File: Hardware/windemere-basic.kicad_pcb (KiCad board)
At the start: 2 copper layers, 152.4 x 158.8 mm, 56 parts, among them J3 Connector, J6 Barrel_Jack, SW1 Reset Button, U1 MCP102-475, U2 HD44780U, U3 WD65C02, U4 28C256, U5 62256, U6 WD65C22, U7 74LS00, U8 MM74C923, U9 L7805, X1 1MHz

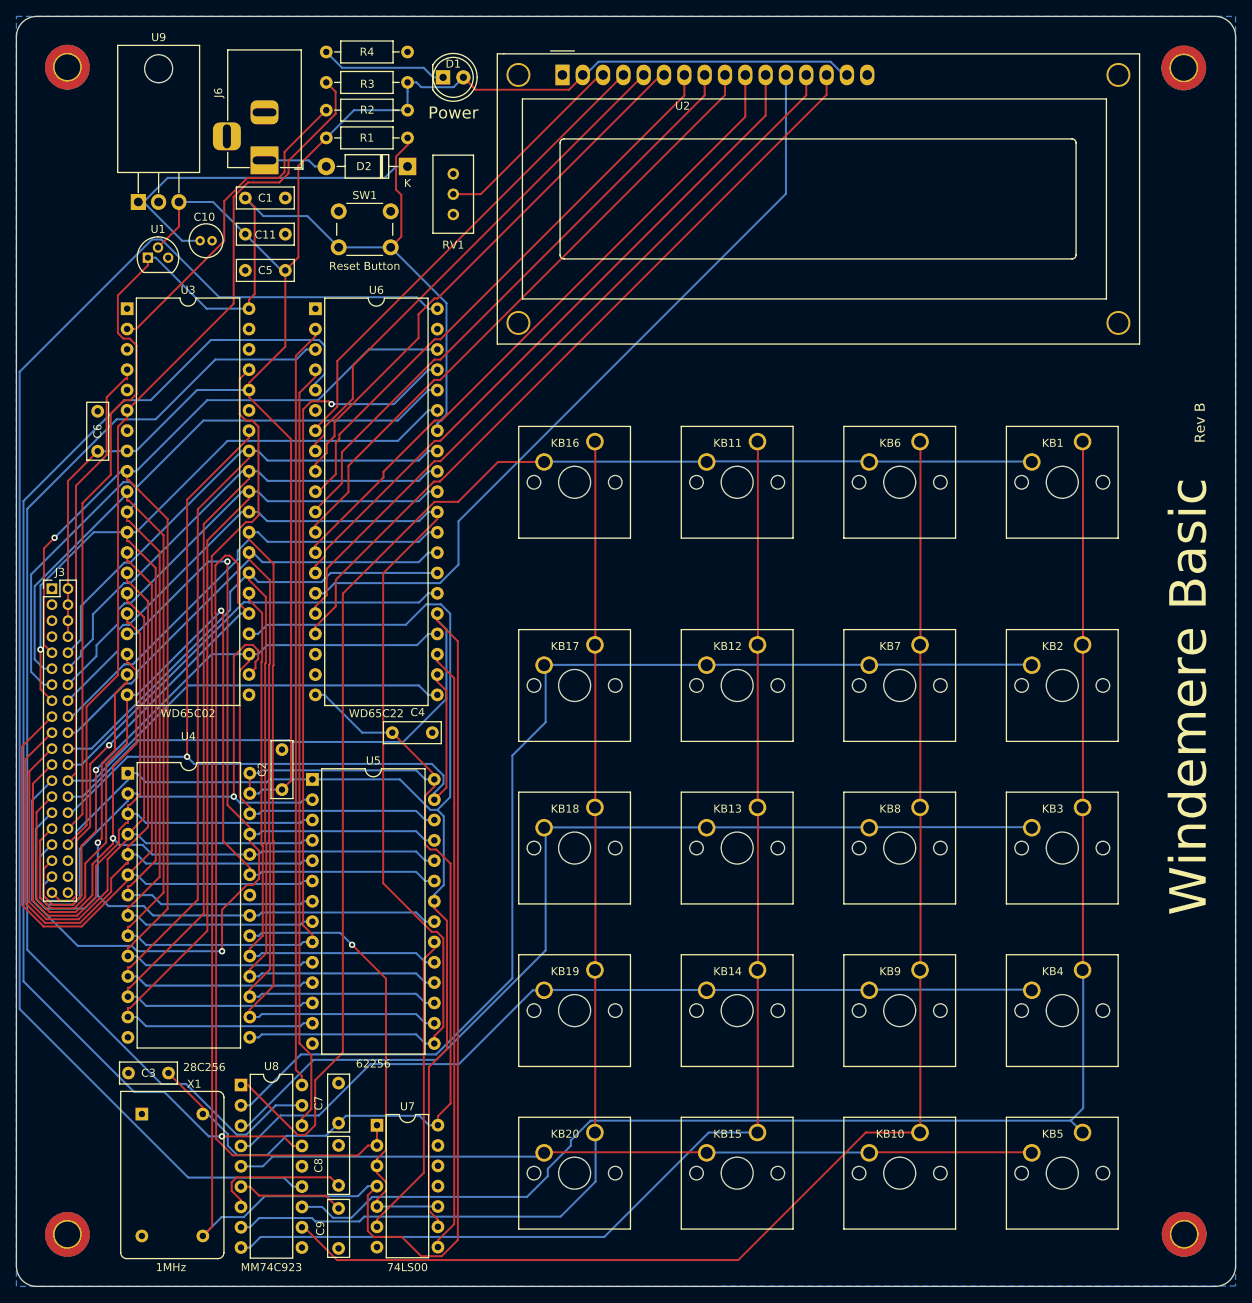
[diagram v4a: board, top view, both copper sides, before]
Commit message: Correct MM74C923
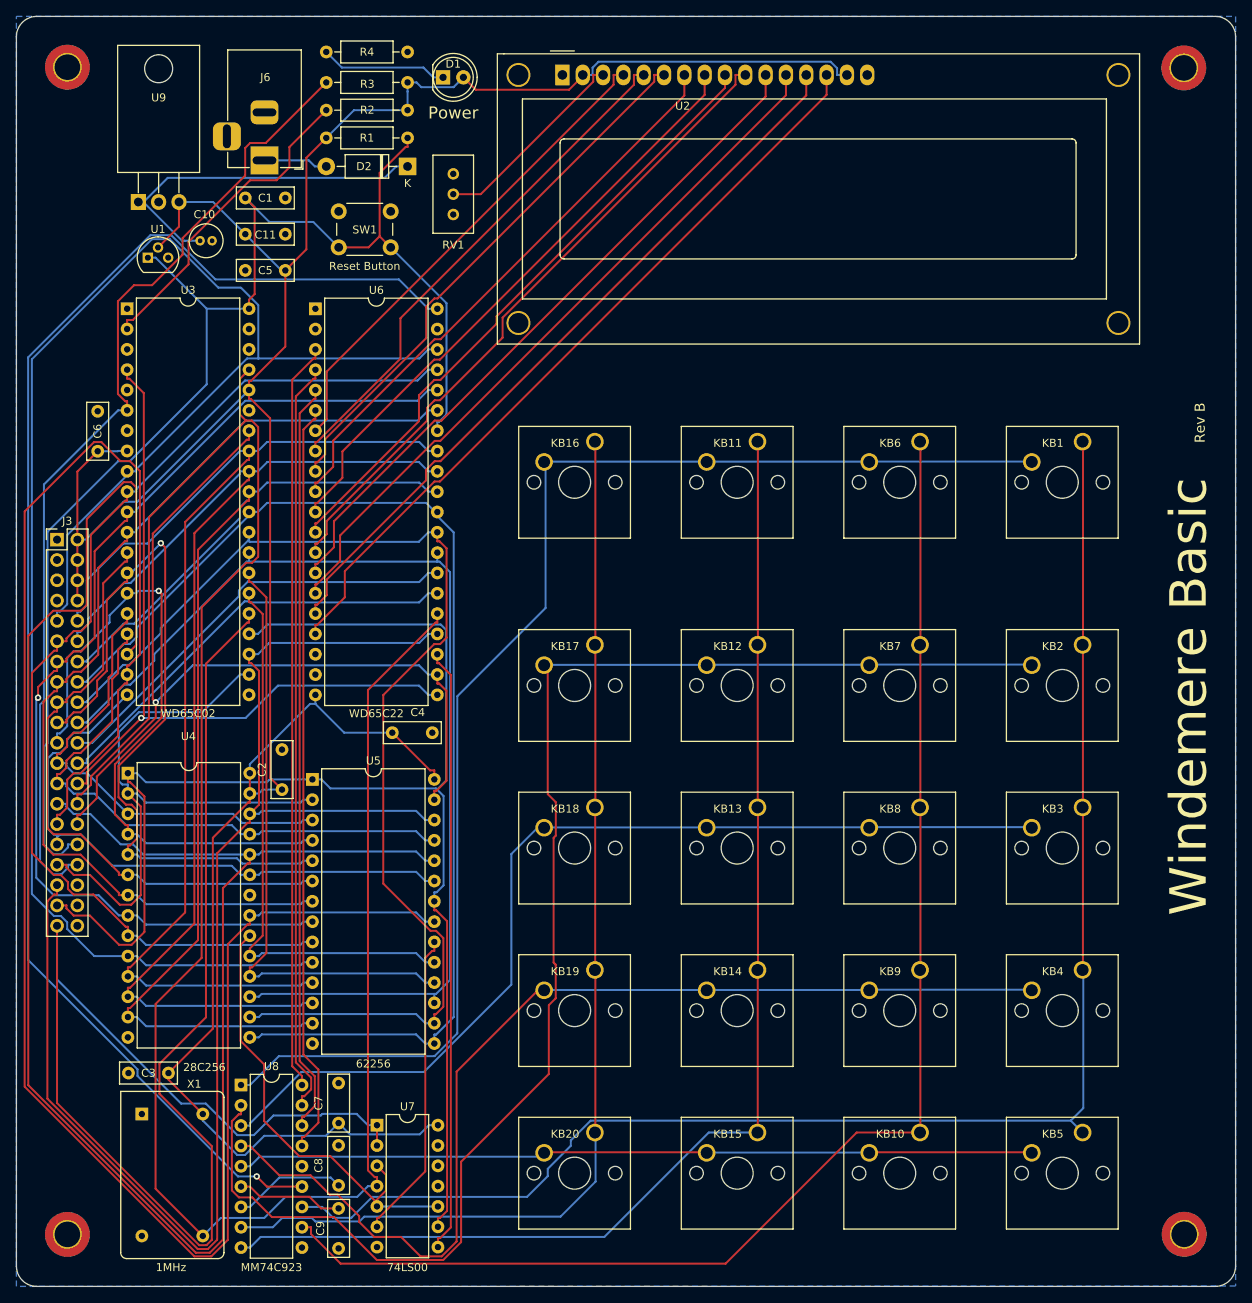
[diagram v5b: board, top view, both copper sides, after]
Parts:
- J3: footprint Connector_PinHeader_2.00mm:PinHeader_2x20_P2.00mm_Vertical -> Connector_PinHeader_2.54mm:PinHeader_2x20_P2.54mm_Vertical
- moved J3 6.16 mm to (138.5, 98.0)
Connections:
- U8 pad 15: Net-(U6-PA3) -> Net-(U6-PA4)
- U8 pad 16: Net-(U6-PA2) -> Net-(U6-PA3)
- U8 pad 17: Net-(U6-PA1) -> Net-(U6-PA2)
- U8 pad 18: Net-(U6-PA0) -> Net-(U6-PA1)
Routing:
- net /A10: track 93.5 -> 241.4 mm, vias 1 -> 0
- net /A9: track 96.8 -> 239.5 mm, vias 1 -> 0
- net Net-(U6-PA0): track 95.8 -> 0.00 mm
- net Net-(U6-PA4): track 0.00 -> 94.5 mm
- net /A8: track 135.1 -> 73.8 mm, vias 2 -> 0
- net Net-(U6-PA3): track 155.7 -> 94.5 mm, vias 1 -> 0
- net /A13: track 121.3 -> 181.4 mm, vias 1 -> 0
- net /A1: track 197.8 -> 138.1 mm, vias 1 -> 0
- net /A0: track 161.6 -> 218.8 mm, vias 1 -> 0
- net Net-(U6-PA1): track 144.8 -> 93.8 mm
- net /A11: track 117.8 -> 75.2 mm, vias 1 -> 0
- net Net-(U8-Y2): track 142.4 -> 183.4 mm
- net /A15: track 154.8 -> 193.9 mm, vias 1 -> 0
- net /A4: track 109.1 -> 76.5 mm
- net /A7: track 90.1 -> 58.5 mm
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
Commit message: correct direction of mm74c923
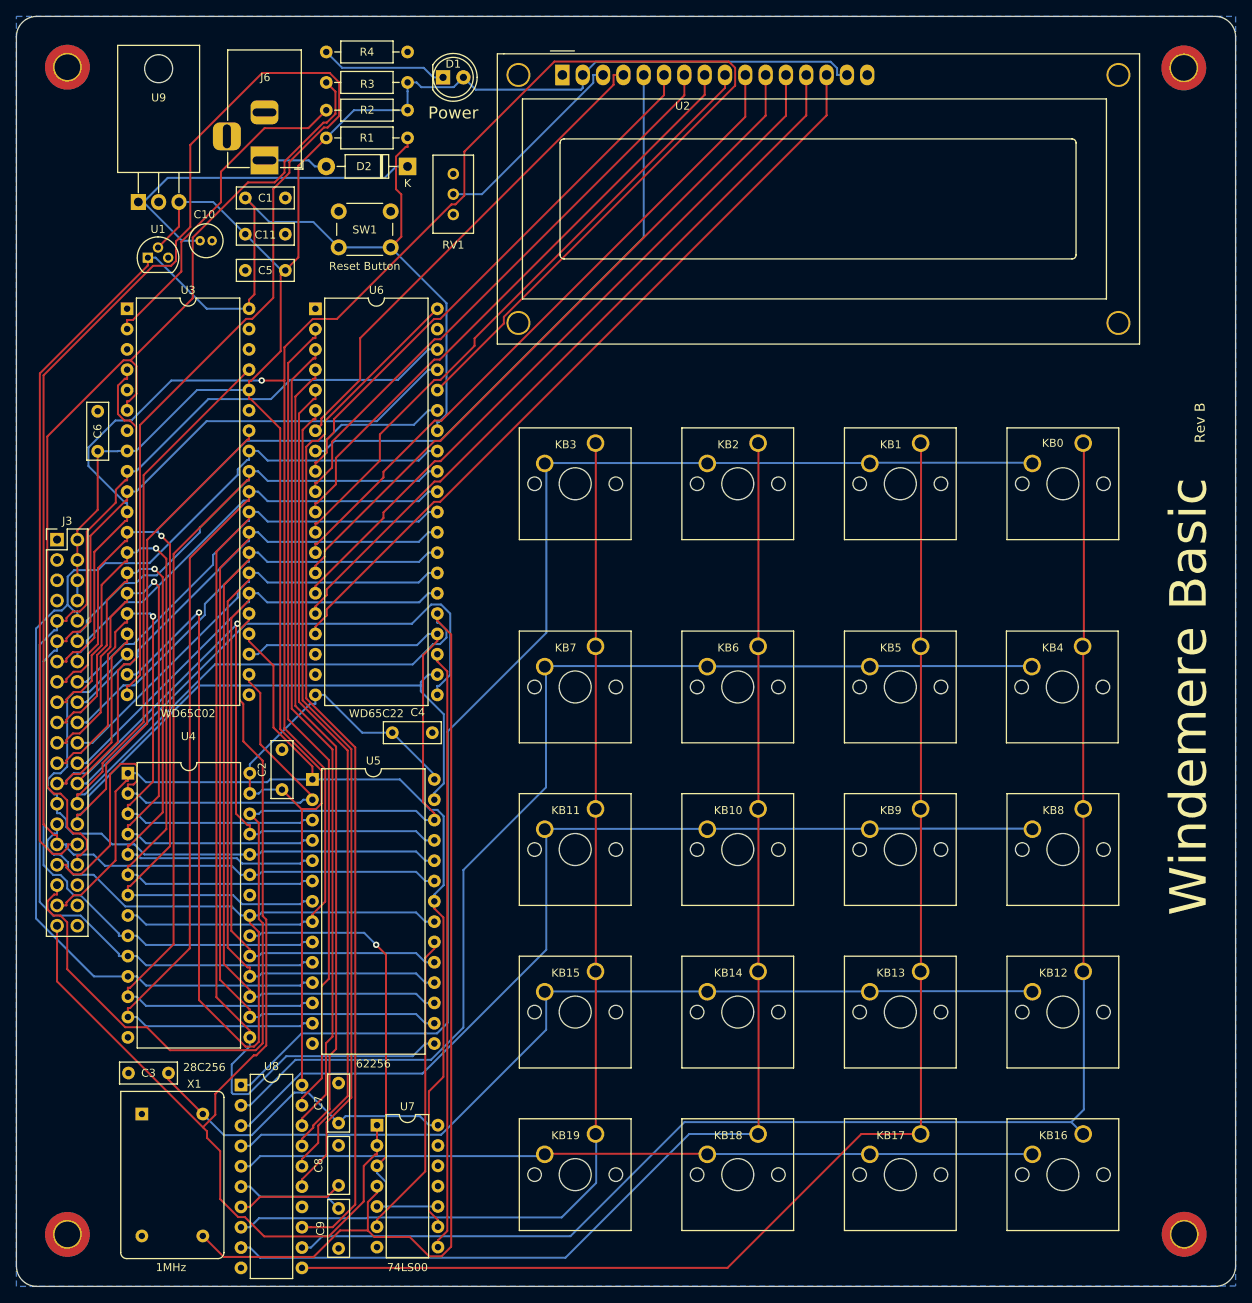
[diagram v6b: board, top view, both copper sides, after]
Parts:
- removed KB20: Push_Button, Button_Switch_Keyboard:SW_Cherry_MX_1.00u_PCB
- added KB0: Push_Button, Button_Switch_Keyboard:SW_Cherry_MX_1.00u_PCB, F.Cu at (266.7, 86.0)
- U8: footprint Package_DIP:DIP-18_W7.62mm -> Package_DIP:DIP-20_W7.62mm
- moved KB16 105.9 mm to (266.7, 172.3)
- moved KB3 76.0 mm to (205.8, 86.0)
- moved KB17 73.5 mm to (246.4, 172.3)
- moved KB5 64.1 mm to (246.4, 111.4)
- moved KB12 57.7 mm to (266.7, 152.0)
- moved KB11 50.2 mm to (205.8, 131.7)
- moved KB2 47.8 mm to (226.1, 86.0)
- moved KB18 45.6 mm to (226.1, 172.3)
- moved KB10 45.2 mm to (226.1, 131.7)
- moved KB7 40.6 mm to (205.8, 111.4)
- moved KB4 40.5 mm to (266.6, 111.4)
- moved KB6 32.6 mm to (226.1, 111.4)
- moved KB13 28.9 mm to (246.4, 152.0)
- moved KB15 28.6 mm to (205.8, 152.0)
- moved KB19 20.5 mm to (205.8, 172.3)
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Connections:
- KB1 pad 1: Net-(U8-X1) -> Net-(U8-X2)
- KB10 pad 1: Net-(U8-X2) -> Net-(U8-X3)
- KB10 pad 2: Net-(U8-Y5) -> Net-(U8-Y3)
- KB11 pad 1: Net-(U8-X3) -> Net-(U8-X4)
- KB11 pad 2: Net-(U8-Y1) -> Net-(U8-Y3)
- KB12 pad 1: Net-(U8-X3) -> Net-(U8-X1)
- KB12 pad 2: Net-(U8-Y2) -> Net-(U8-Y4)
- KB13 pad 1: Net-(U8-X3) -> Net-(U8-X2)
- KB13 pad 2: Net-(U8-Y3) -> Net-(U8-Y4)
- KB15 pad 1: Net-(U8-X3) -> Net-(U8-X4)
- KB15 pad 2: Net-(U8-Y5) -> Net-(U8-Y4)
- KB16 pad 1: Net-(U8-X4) -> Net-(U8-X1)
- KB16 pad 2: Net-(U8-Y1) -> Net-(U8-Y5)
- KB17 pad 1: Net-(U8-X4) -> Net-(U8-X2)
- KB17 pad 2: Net-(U8-Y2) -> Net-(U8-Y5)
- KB18 pad 1: Net-(U8-X4) -> Net-(U8-X3)
- KB18 pad 2: Net-(U8-Y3) -> Net-(U8-Y5)
- KB19 pad 2: Net-(U8-Y4) -> Net-(U8-Y5)
- KB2 pad 1: Net-(U8-X1) -> Net-(U8-X3)
- KB2 pad 2: Net-(U8-Y2) -> Net-(U8-Y1)
- KB3 pad 1: Net-(U8-X1) -> Net-(U8-X4)
- KB3 pad 2: Net-(U8-Y3) -> Net-(U8-Y1)
- KB4 pad 2: Net-(U8-Y4) -> Net-(U8-Y2)
- KB5 pad 1: Net-(U8-X1) -> Net-(U8-X2)
- KB5 pad 2: Net-(U8-Y5) -> Net-(U8-Y2)
- KB6 pad 1: Net-(U8-X2) -> Net-(U8-X3)
- KB6 pad 2: Net-(U8-Y1) -> Net-(U8-Y2)
- KB7 pad 1: Net-(U8-X2) -> Net-(U8-X4)
- KB8 pad 1: Net-(U8-X2) -> Net-(U8-X1)
- KB9 pad 2: Net-(U8-Y4) -> Net-(U8-Y3)
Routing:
- net /A11: track 75.2 -> 258.1 mm
- net /A9: track 239.5 -> 76.8 mm
- net /A2: track 134.4 -> 290.5 mm
- net Net-(U6-PA0): track 0.00 -> 102.1 mm
- net /A10: track 241.4 -> 143.7 mm, vias 0 -> 1
- net /A0: track 218.8 -> 142.7 mm
- net Net-(U6-CA1): track 183.1 -> 129.6 mm, vias 1 -> 0
- net /A15: track 193.9 -> 144.2 mm
- net Net-(U8-Y2): track 183.4 -> 142.2 mm
- net /A14: track 177.4 -> 138.5 mm
- net /A13: track 181.4 -> 143.9 mm
- net Net-(J3-Pin_28): track 275.5 -> 243.6 mm
- net /A8: track 73.8 -> 105.6 mm, vias 0 -> 1
- net Net-(J3-Pin_26): track 96.1 -> 124.6 mm, vias 1 -> 0
- net Net-(U8-Y4): track 131.3 -> 110.0 mm
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
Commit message: Add Bypass to 74LS923
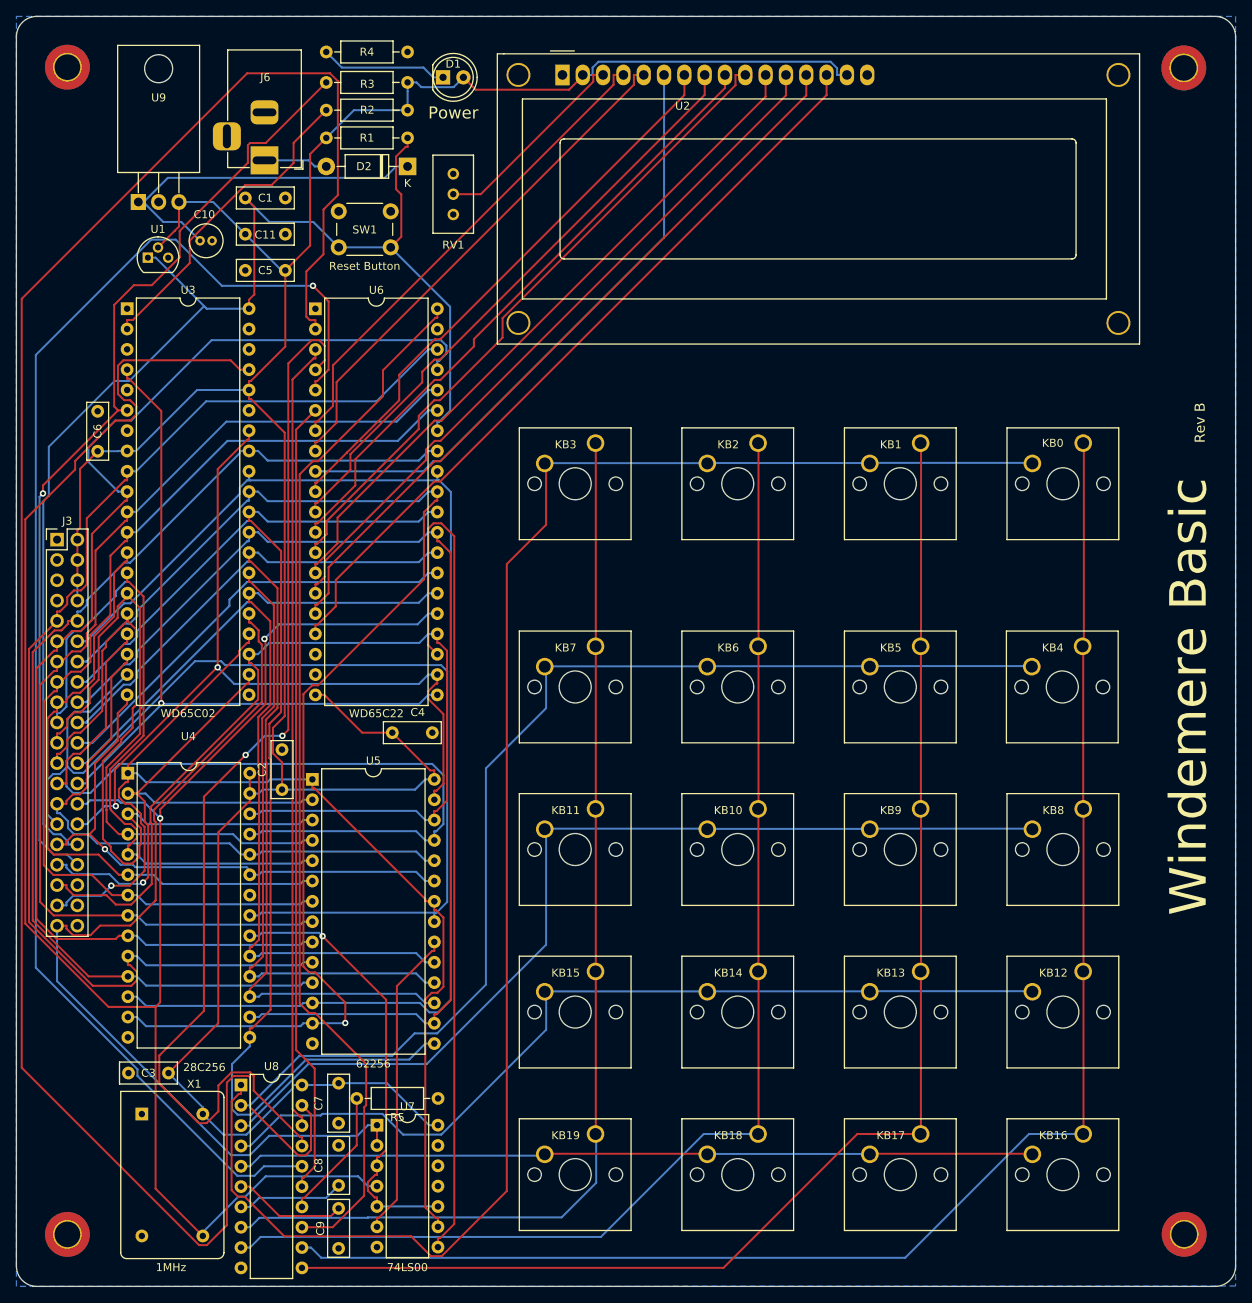
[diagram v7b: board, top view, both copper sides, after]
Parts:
- added R5: 1K, Resistor_THT:R_Axial_DIN0207_L6.3mm_D2.5mm_P10.16mm_Horizontal, F.Cu at (186.1, 167.9)
- moved C7 4.99 mm to (173.7, 166.0), turned to -90 degrees
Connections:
- U8 pad 14: GND -> Net-(U8-XOE)
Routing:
- net /A11: track 258.1 -> 70.6 mm, vias 0 -> 1
- net Net-(U6-PA0): track 102.1 -> 258.4 mm
- net /A2: track 290.5 -> 135.3 mm, vias 1 -> 0
- net Net-(U6-PA3): track 102.9 -> 179.3 mm, vias 0 -> 1
- net Net-(U8-Y1): track 165.2 -> 209.1 mm
- net Net-(U6-PA2): track 102.1 -> 137.5 mm, vias 0 -> 2
- net Net-(U6-~{CS2}): track 75.1 -> 110.2 mm
- net Net-(J3-Pin_26): track 124.6 -> 93.6 mm, vias 0 -> 1
- net /A15: track 144.2 -> 117.2 mm
- net Net-(J3-Pin_30): track 128.8 -> 106.3 mm, vias 0 -> 2
- net /A1: track 136.2 -> 158.4 mm
- net /A13: track 143.9 -> 122.1 mm
- net /A4: track 94.7 -> 77.8 mm, vias 1 -> 0
- net Net-(U8-XOE): track 0.00 -> 16.6 mm
- net Net-(J3-Pin_28): track 243.6 -> 258.6 mm, vias 0 -> 2
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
